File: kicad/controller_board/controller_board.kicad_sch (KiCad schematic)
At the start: 9 parts, among them J1 Battery Conn, Q1 FQP27P06, SW1 On/Off, SW2 Pair/Direction, U1 ESP32-C3-SuperMini

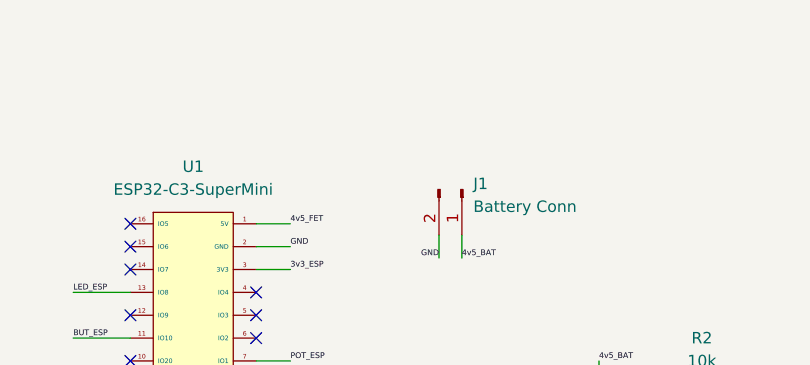
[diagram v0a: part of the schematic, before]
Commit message: Update GPIO assignments and complete first-pass PCB layout
Swap motor control IN1/IN2 pins to simplify PCB routing:
- Motor 1: IN1 GPIO4, IN2 GPIO3 (was IN1 GPIO3, IN2 GPIO4)
- Motor 2: IN1 GPIO7, IN2 GPIO6 (was IN1 GPIO6, IN2 GPIO7)

Updated documentation:
- lib/hardware.py: Motor GPIO pin definitions
- README.md: Receiver GPIO assignment table
- receiver/README.md: Hardware pin descriptions

PCB design progress:
- Controller board: First-pass layout and routing complete
- Receiver logic board: First-pass layout and routing complete
- Receiver power board: First-pass layout and routing complete
- All decoupling capacitors added (470µF on TB6612 VM, 0.1µF on logic)
- Verified netlists: power, ground, GPIO, and board-to-board connections

Design notes:
- Potentiometer uses pin socket for off-board panel mount (bent legs)
- P-FET uses bent legs for mechanical positioning in enclosure
- P-FET on logic board near high-current loads (smart placement)
- Board-to-board connector properly routes all 6 signals

Co-Authored-By: Claude Sonnet 4.5 <noreply@anthropic.com>
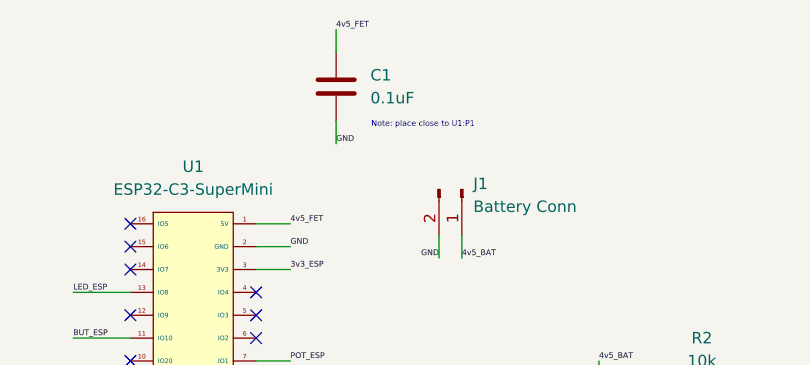
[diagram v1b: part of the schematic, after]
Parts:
- added C1: 0.1uF, Capacitor_THT:C_Disc_D5.0mm_W2.5mm_P5.00mm, symbol Device:C
- J1: footprint Connector_PinHeader_2.54mm:PinHeader_1x02_P2.54mm_Horizontal -> Connector_PinHeader_2.54mm:PinHeader_1x02_P2.54mm_Vertical
- RV1: footprint Potentiometer_THT:Potentiometer_Alps_RK163_Single_Horizontal -> Connector_PinSocket_2.54mm:PinSocket_1x03_P2.54mm_Vertical
- SW2: footprint (none) -> ESP32_Lego_PF:Push_Button_TSD016
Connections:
- net 4v5_FET: now also C1.1
- net GND: now also C1.2
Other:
- note added: "Note: place close to U1:P1"
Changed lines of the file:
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@@
 	(generator_version "9.0")
 	(paper "A4")
+	(text "Note: place close to U1:P1"
+		(exclude_from_sim no)
+		(at 174.752 43.688 0)
+		(effects
+			(font
+				(size 0.635 0.635)
+			)
+		)
+	)
 	(junction
 		(at 194.31 73.66)
@@
 	(wire
 		(pts
+			(xy 165.1 33.02) (xy 165.1 35.56)
+		)
+		(stroke
+			(width 0)
+			(type default)
+		)
+	)
+	(wire
+		(pts
 			(xy 135.89 67.31) (xy 142.24 67.31)
 		)
@@
 		(pts
 			(xy 179.07 58.42) (xy 179.07 55.88)
+		)
+		(stroke
+			(width 0)
+			(type default)
+		)
+	)
+	(wire
+		(pts
+			(xy 165.1 45.72) (xy 165.1 43.18)
 		)
 		(stroke
@@
 		)
 	)
+	(label "GND"
+		(at 165.1 45.72 0)
+		(effects
+			(font
+				(size 0.635 0.635)
+			)
+			(justify left bottom)
+		)
+	)
 	(label "4v5_BAT"
 		(at 194.31 69.85 0)
@@
 			)
 			(justify right bottom)
+		)
+	)
+	(label "4v5_FET"
+		(at 165.1 33.02 0)
+		(effects
+			(font
+				(size 0.635 0.635)
+			)
+			(justify left bottom)
 		)
 	)
@@
 			)
 		)
-		(property "Footprint" "Potentiometer_THT:Potentiometer_Alps_RK163_Single_Horizontal"
+		(property "Footprint" "Connector_PinSocket_2.54mm:PinSocket_1x03_P2.54mm_Vertical"
 			(at 147.32 92.71 0)
 			(effects
@@
 				(path "/e1aa1564-c9a0-424d-a4fc-995e6922032c"
 					(reference "RV1")
+					(unit 1)
+				)
+			)
+		)
+	)
+	(symbol
+		(lib_id "Device:C")
+		(at 165.1 39.37 0)
+		(unit 1)
+		(exclude_from_sim no)
+		(in_bom yes)
+		(on_board yes)
+		(dnp no)
+		(fields_autoplaced yes)
+		(property "Reference" "C1"
+			(at 168.91 38.0999 0)
+			(effects
+				(font
+					(size 1.27 1.27)
+				)
+				(justify left)
+			)
+		)
+		(property "Value" "0.1uF"
+			(at 168.91 40.6399 0)
+			(effects
+				(font
+					(size 1.27 1.27)
+				)
+				(justify left)
+			)
+		)
+		(property "Footprint" "Capacitor_THT:C_Disc_D5.0mm_W2.5mm_P5.00mm"
+			(at 166.0652 43.18 0)
+			(effects
+				(font
+					(size 1.27 1.27)
+				)
+				(hide yes)
+			)
+		)
+		(property "Datasheet" "~"
+			(at 165.1 39.37 0)
+			(effects
+				(font
+					(size 1.27 1.27)
+				)
+				(hide yes)
+			)
+		)
+		(property "Description" "Unpolarized capacitor"
+			(at 165.1 39.37 0)
+			(effects
+				(font
+					(size 1.27 1.27)
+				)
+				(hide yes)
+			)
+		)
+		(pin "1"
+		)
+		(pin "2"
+		)
+		(instances
+			(project "controller_board"
+				(path "/e1aa1564-c9a0-424d-a4fc-995e6922032c"
+					(reference "C1")
 					(unit 1)
 				)
@@
 			)
 		)
-		(property "Footprint" ""
+		(property "Footprint" "ESP32_Lego_PF:Push_Button_TSD016"
 			(at 109.22 90.17 0)
 			(effects
@@
 			)
 		)
-		(property "Footprint" "Connector_PinHeader_2.54mm:PinHeader_1x02_P2.54mm_Horizontal"
+		(property "Footprint" "Connector_PinHeader_2.54mm:PinHeader_1x02_P2.54mm_Vertical"
 			(at 179.07 50.8 0)
 			(effects
